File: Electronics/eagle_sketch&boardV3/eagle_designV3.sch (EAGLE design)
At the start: 16 parts, among them IC1 7805L

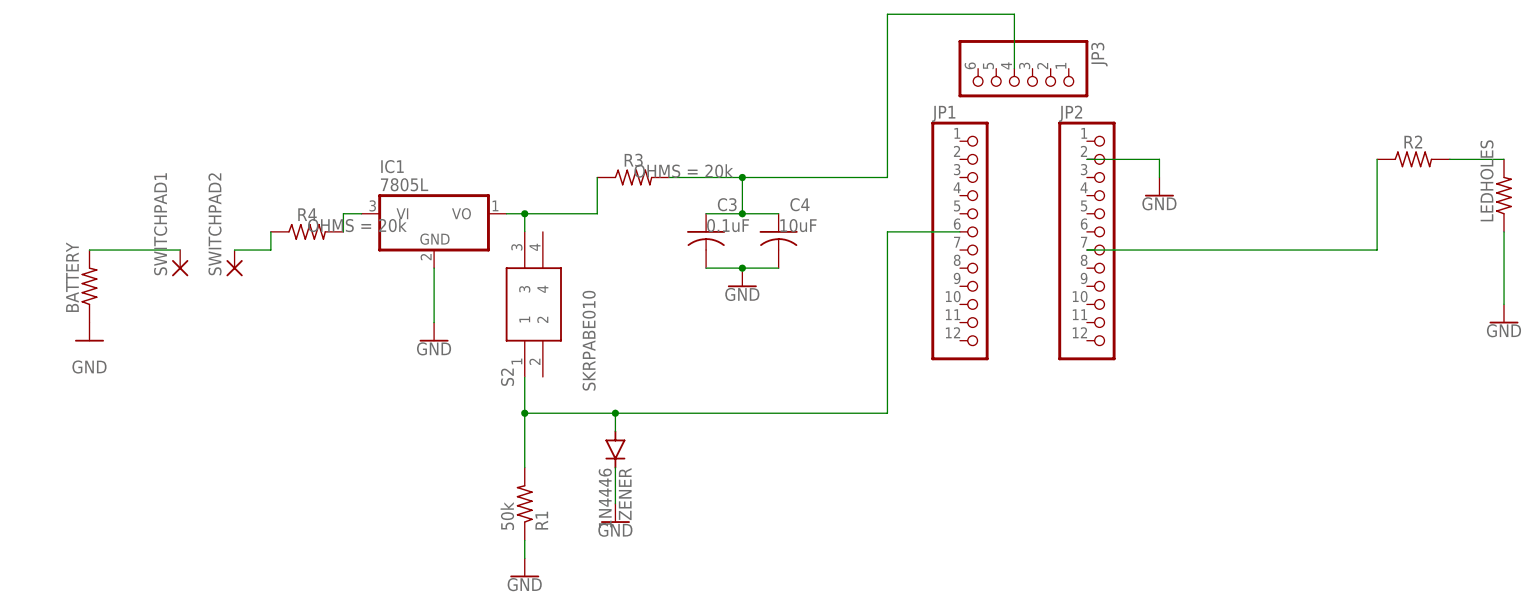
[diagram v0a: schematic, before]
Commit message: updated board and schematic with post review suggestions from Issue 30
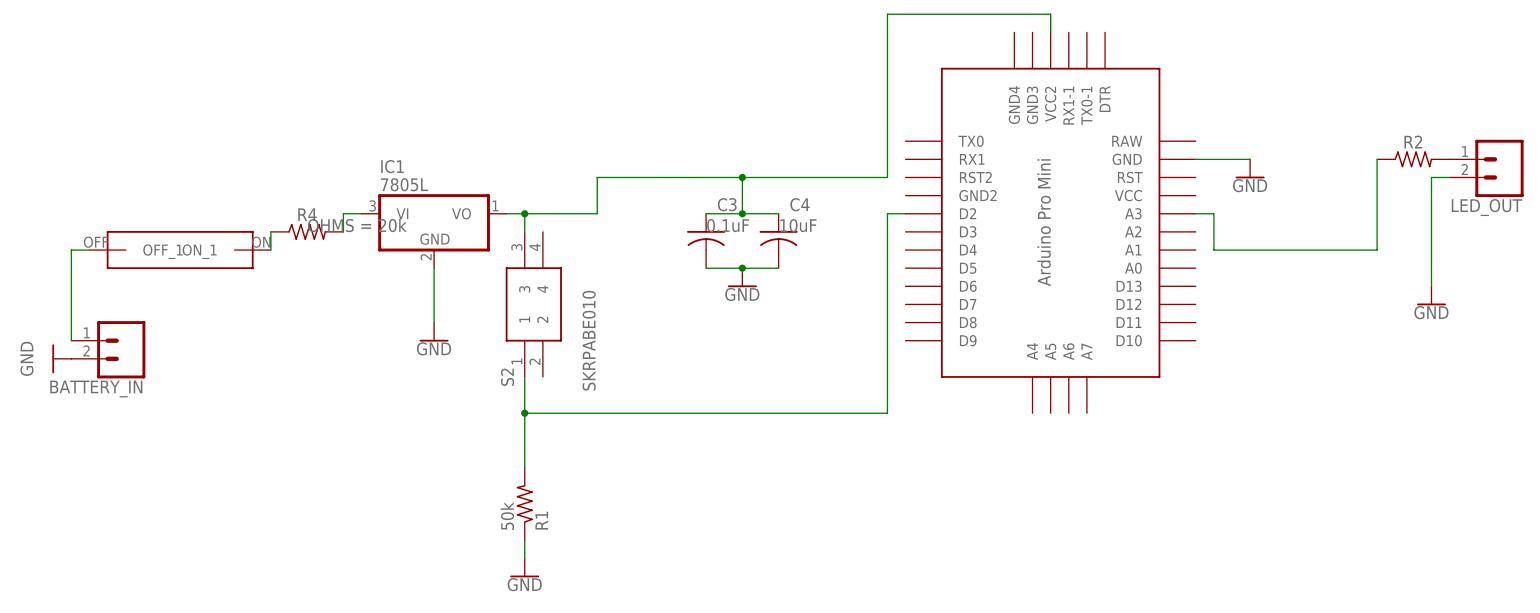
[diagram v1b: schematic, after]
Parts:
- removed BATTERY: (no value), adafruit:R-US_0411/12
- removed JP1, JP2: (no value), adafruit:PINHD-1X12
- removed JP3: (no value), adafruit:PINHD-1X6
- removed LEDHOLES: (no value), adafruit:R-US_0309/12
- removed R3: 20k, adafruit:R-US_R0805
- removed SWITCHPAD1, SWITCHPAD2: (no value), wirepad:SMD2
- removed ZENER: 1N4446, diode:1N4446
- added BATTERY_IN, LED_OUT: (no value), SparkFun-Connectors:CONN_02
- added U$1: PRO-MINI, Arduino-clone:PRO-MINI
- added U$2: SDA01H1SBD_DEVICE, DIPswitchLib:SDA01H1SBD_DEVICE
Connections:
- removed net N$6: C3.1, C4.1, JP3.4, R3.2
- removed net N$9: LEDHOLES.2, R2.2
- new net N$7: LED_OUT.1, R2.2
- net GND: now also BATTERY_IN.2, LED_OUT.2, U$1.GND; no longer BATTERY.1, JP2.2, LEDHOLES.1, ZENER.C
- net N$1: now also BATTERY_IN.1, U$2.OFF_1; no longer BATTERY.2, SWITCHPAD1.P
- net N$2: now also U$2.ON_1; no longer SWITCHPAD2.P
- net N$4: now also C3.1, C4.1, U$1.VCC2; no longer R3.1
- net N$5: now also U$1.D2; no longer JP1.6, ZENER.A
- net N$8: now also U$1.A3; no longer JP2.7

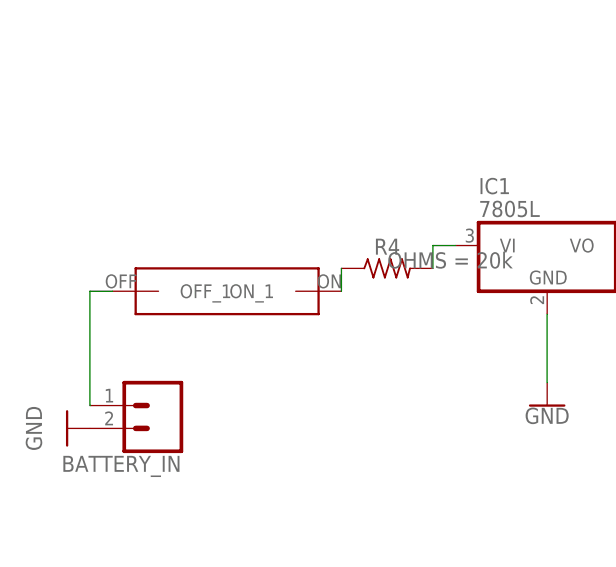
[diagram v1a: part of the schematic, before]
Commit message: updated board to reflect toggle switch change
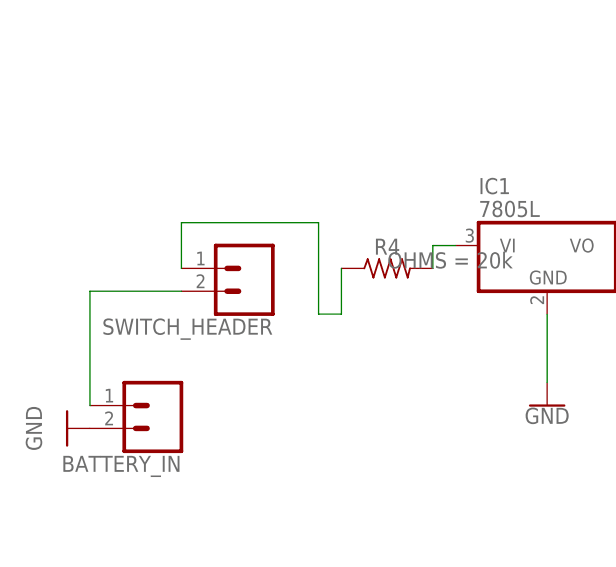
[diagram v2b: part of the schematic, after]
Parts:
- removed U$2: SDA01H1SBD_DEVICE, DIPswitchLib:SDA01H1SBD_DEVICE
- added SWITCH_HEADER: (no value), SparkFun-Connectors:CONN_02
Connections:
- net N$1: now also SWITCH_HEADER.2; no longer U$2.OFF_1
- net N$2: now also SWITCH_HEADER.1; no longer U$2.ON_1
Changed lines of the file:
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@@
 <part name="GND6" library="SparkFun-PowerSymbols" library_urn="urn:adsk.eagle:library:530" deviceset="GND" device=""/>
 <part name="U$1" library="Arduino-clone" deviceset="PRO-MINI" device=""/>
-<part name="U$2" library="DIPswitchLib" deviceset="SDA01H1SBD_DEVICE" device=""/>
 <part name="BATTERY_IN" library="SparkFun-Connectors" library_urn="urn:adsk.eagle:library:513" deviceset="CONN_02" device="" package3d_urn="urn:adsk.eagle:package:38039/1"/>
 <part name="LED_OUT" library="SparkFun-Connectors" library_urn="urn:adsk.eagle:library:513" deviceset="CONN_02" device="" package3d_urn="urn:adsk.eagle:package:38039/1"/>
+<part name="SWITCH_HEADER" library="SparkFun-Connectors" library_urn="urn:adsk.eagle:library:513" deviceset="CONN_02" device="" package3d_urn="urn:adsk.eagle:package:38039/1"/>
 </parts>
 <sheets>
@@
 </instance>
 <instance part="U$1" gate="G$1" x="144.78" y="53.34" smashed="yes"/>
-<instance part="U$2" gate="G$1" x="20.32" y="58.42" smashed="yes"/>
 <instance part="BATTERY_IN" gate="G$1" x="12.7" y="45.72" smashed="yes" rot="R180">
 <attribute name="VALUE" x="15.24" y="50.546" size="1.778" layer="96" font="vector" rot="R180"/>
@@
 <attribute name="NAME" x="208.28" y="65.532" size="1.778" layer="95" font="vector" rot="R180"/>
 </instance>
+<instance part="SWITCH_HEADER" gate="G$1" x="22.86" y="60.96" smashed="yes" rot="R180">
+<attribute name="VALUE" x="25.4" y="65.786" size="1.778" layer="96" font="vector" rot="R180"/>
+<attribute name="NAME" x="25.4" y="55.372" size="1.778" layer="95" font="vector" rot="R180"/>
+</instance>
 </instances>
 <busses>
@@
 <segment>
 <pinref part="R4" gate="G$1" pin="1"/>
-<wire x1="33.02" y1="58.42" x2="33.02" y2="60.96" width="0.1524" layer="91"/>
-<pinref part="U$2" gate="G$1" pin="ON_1"/>
+<pinref part="SWITCH_HEADER" gate="G$1" pin="1"/>
+<wire x1="15.24" y1="60.96" x2="15.24" y2="66.04" width="0.1524" layer="91"/>
+<wire x1="15.24" y1="66.04" x2="30.48" y2="66.04" width="0.1524" layer="91"/>
+<wire x1="30.48" y1="66.04" x2="30.48" y2="55.88" width="0.1524" layer="91"/>
+<wire x1="30.48" y1="55.88" x2="33.02" y2="55.88" width="0.1524" layer="91"/>
+<wire x1="33.02" y1="55.88" x2="33.02" y2="60.96" width="0.1524" layer="91"/>
 </segment>
 </net>
@@
 <pinref part="BATTERY_IN" gate="G$1" pin="1"/>
 <wire x1="5.08" y1="45.72" x2="5.08" y2="58.42" width="0.1524" layer="91"/>
-<pinref part="U$2" gate="G$1" pin="OFF_1"/>
-<wire x1="5.08" y1="58.42" x2="7.62" y2="58.42" width="0.1524" layer="91"/>
+<pinref part="SWITCH_HEADER" gate="G$1" pin="2"/>
+<wire x1="5.08" y1="58.42" x2="15.24" y2="58.42" width="0.1524" layer="91"/>
 </segment>
 </net>

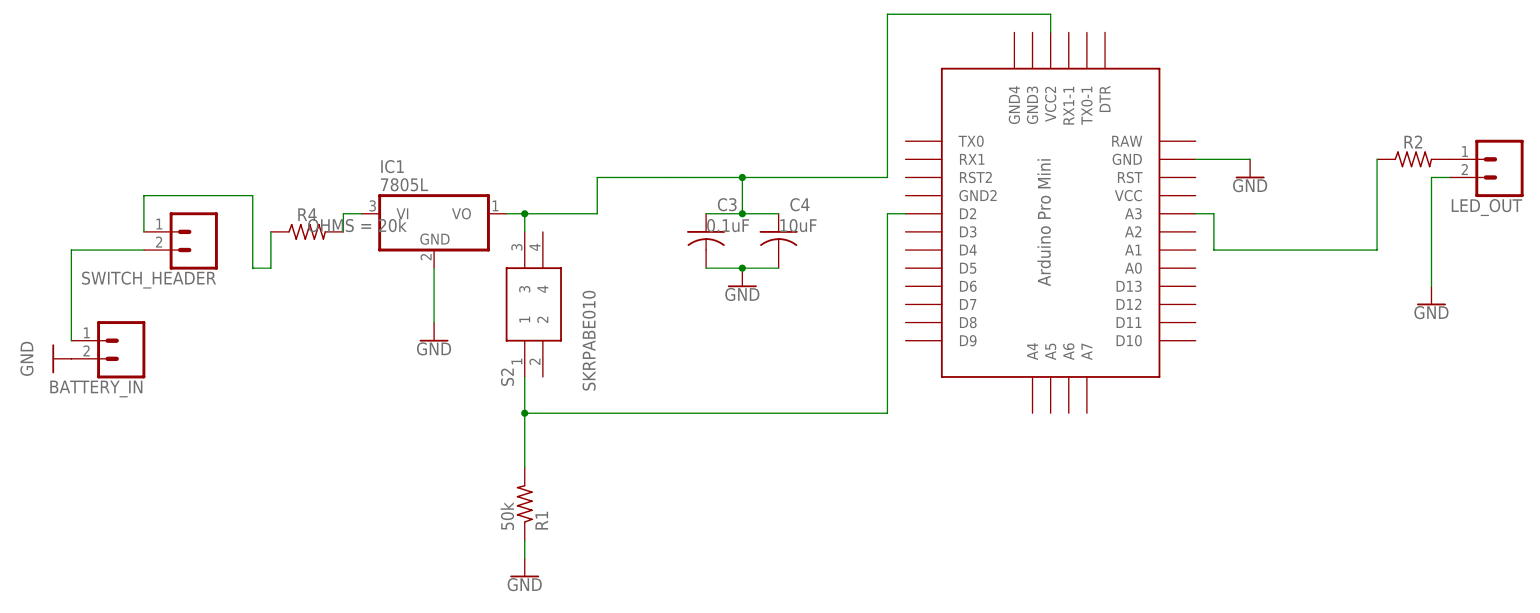
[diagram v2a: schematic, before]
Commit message: updated board and schematic to reflect removal of resistor btwn battery and voltage reg
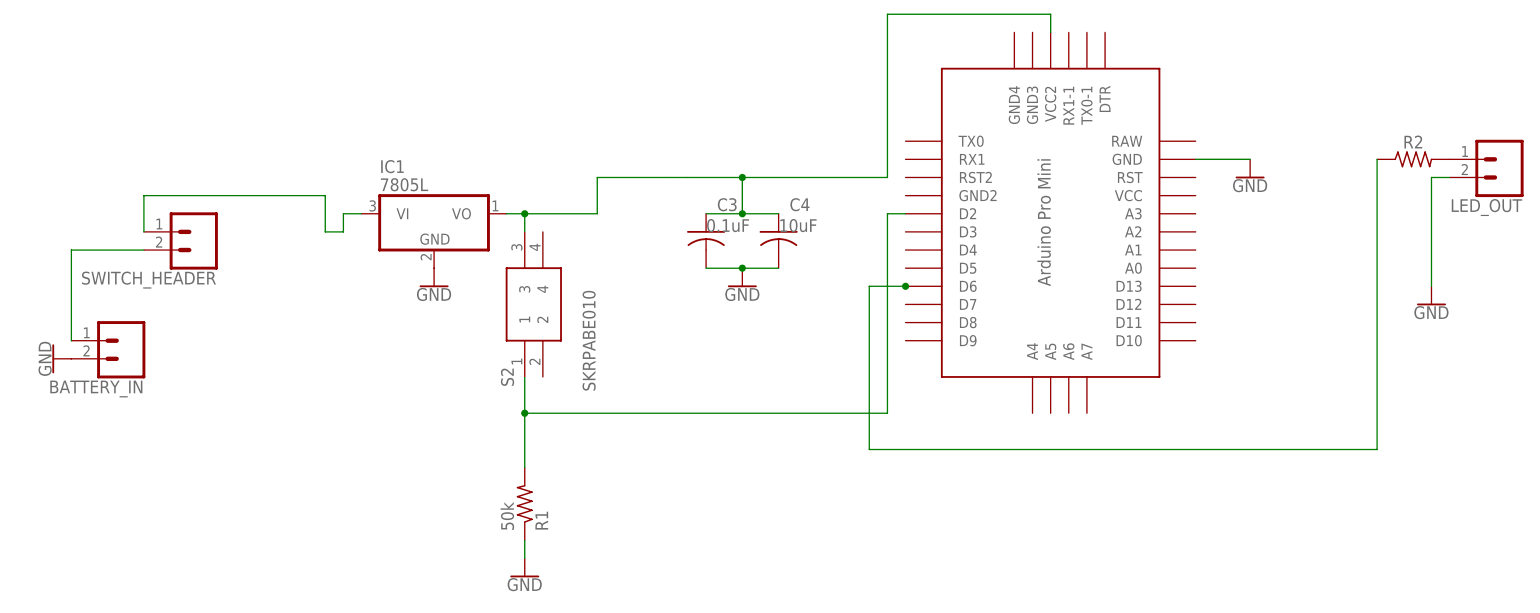
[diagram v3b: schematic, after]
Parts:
- removed R4: 20k, adafruit:R-US_R0805
- R2: value 1.5k -> 330
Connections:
- removed net N$3: IC1.VI, R4.2
- removed net N$8: R2.1, U$1.A3
- new net N$6: R2.1, U$1.D6
- net N$2: now also IC1.VI; no longer R4.1
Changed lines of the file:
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@@
 <part name="R1" library="adafruit" library_urn="urn:adsk.eagle:library:420" deviceset="R-US_" device="R0805" package3d_urn="urn:adsk.eagle:package:6240566/1" value="50k"/>
 <part name="S2" library="SKRPABE010" deviceset="SKRPABE010" device=""/>
-<part name="R2" library="adafruit" library_urn="urn:adsk.eagle:library:420" deviceset="R-US_" device="R0805" package3d_urn="urn:adsk.eagle:package:6240566/1" value="1.5k"/>
-<part name="GND1" library="SparkFun-PowerSymbols" library_urn="urn:adsk.eagle:library:530" deviceset="GND" device=""/>
-<part name="R4" library="adafruit" library_urn="urn:adsk.eagle:library:420" deviceset="R-US_" device="R0805" package3d_urn="urn:adsk.eagle:package:6240566/1" value="20k">
-<attribute name="OHMS" value="20k"/>
-</part>
+<part name="R2" library="adafruit" library_urn="urn:adsk.eagle:library:420" deviceset="R-US_" device="R0805" package3d_urn="urn:adsk.eagle:package:6240566/1" value="330"/>
 <part name="GND4" library="SparkFun-PowerSymbols" library_urn="urn:adsk.eagle:library:530" deviceset="GND" device=""/>
 <part name="C3" library="adafruit" library_urn="urn:adsk.eagle:library:420" deviceset="C-US" device="C0805" package3d_urn="urn:adsk.eagle:package:6240337/1" value="0.1uF">
@@
 <part name="LED_OUT" library="SparkFun-Connectors" library_urn="urn:adsk.eagle:library:513" deviceset="CONN_02" device="" package3d_urn="urn:adsk.eagle:package:38039/1"/>
 <part name="SWITCH_HEADER" library="SparkFun-Connectors" library_urn="urn:adsk.eagle:library:513" deviceset="CONN_02" device="" package3d_urn="urn:adsk.eagle:package:38039/1"/>
+<part name="GND1" library="SparkFun-PowerSymbols" library_urn="urn:adsk.eagle:library:530" deviceset="GND" device=""/>
 </parts>
 <sheets>
@@
 <instance part="R2" gate="G$1" x="193.04" y="71.12" smashed="yes">
 <attribute name="NAME" x="193.04" y="72.644" size="1.778" layer="95" font="vector" align="bottom-center"/>
-</instance>
-<instance part="GND1" gate="1" x="2.54" y="43.18" smashed="yes" rot="R270">
-<attribute name="VALUE" x="-0.254" y="43.18" size="1.778" layer="96" rot="R270" align="top-center"/>
-</instance>
-<instance part="R4" gate="G$1" x="38.1" y="60.96" smashed="yes">
-<attribute name="NAME" x="38.1" y="62.484" size="1.778" layer="95" font="vector" align="bottom-center"/>
-<attribute name="OHMS" x="38.1" y="60.96" size="1.778" layer="96" display="both"/>
 </instance>
 <instance part="GND4" gate="1" x="68.58" y="12.7" smashed="yes">
@@
 <attribute name="VALUE" x="48.26" y="66.675" size="1.778" layer="96"/>
 </instance>
-<instance part="GND3" gate="1" x="55.88" y="45.72" smashed="yes">
-<attribute name="VALUE" x="55.88" y="45.466" size="1.778" layer="96" align="top-center"/>
+<instance part="GND3" gate="1" x="55.88" y="53.34" smashed="yes">
+<attribute name="VALUE" x="55.88" y="53.086" size="1.778" layer="96" align="top-center"/>
 </instance>
 <instance part="GND6" gate="1" x="99.06" y="53.34" smashed="yes">
@@
 <attribute name="NAME" x="25.4" y="55.372" size="1.778" layer="95" font="vector" rot="R180"/>
 </instance>
+<instance part="GND1" gate="1" x="2.54" y="43.18" smashed="yes" rot="R270">
+<attribute name="VALUE" x="2.286" y="43.18" size="1.778" layer="96" rot="R270" align="top-center"/>
+</instance>
 </instances>
 <busses>
@@
 <net name="N$2" class="0">
 <segment>
-<pinref part="R4" gate="G$1" pin="1"/>
 <pinref part="SWITCH_HEADER" gate="G$1" pin="1"/>
 <wire x1="15.24" y1="60.96" x2="15.24" y2="66.04" width="0.1524" layer="91"/>
-<wire x1="15.24" y1="66.04" x2="30.48" y2="66.04" width="0.1524" layer="91"/>
-<wire x1="30.48" y1="66.04" x2="30.48" y2="55.88" width="0.1524" layer="91"/>
-<wire x1="30.48" y1="55.88" x2="33.02" y2="55.88" width="0.1524" layer="91"/>
-<wire x1="33.02" y1="55.88" x2="33.02" y2="60.96" width="0.1524" layer="91"/>
-</segment>
-</net>
-<net name="N$3" class="0">
-<segment>
+<wire x1="15.24" y1="66.04" x2="40.64" y2="66.04" width="0.1524" layer="91"/>
+<wire x1="40.64" y1="66.04" x2="40.64" y2="60.96" width="0.1524" layer="91"/>
 <pinref part="IC1" gate="A1" pin="VI"/>
-<pinref part="R4" gate="G$1" pin="2"/>
 <wire x1="45.72" y1="63.5" x2="43.18" y2="63.5" width="0.1524" layer="91"/>
 <wire x1="43.18" y1="63.5" x2="43.18" y2="60.96" width="0.1524" layer="91"/>
+<wire x1="40.64" y1="60.96" x2="43.18" y2="60.96" width="0.1524" layer="91"/>
 </segment>
 </net>
 <net name="GND" class="0">
-<segment>
-<pinref part="IC1" gate="A1" pin="GND"/>
-<pinref part="GND3" gate="1" pin="GND"/>
-<wire x1="55.88" y1="55.88" x2="55.88" y2="48.26" width="0.1524" layer="91"/>
-</segment>
 <segment>
 <pinref part="R1" gate="G$1" pin="1"/>
@@
 </segment>
 <segment>
-<pinref part="BATTERY_IN" gate="G$1" pin="2"/>
-<pinref part="GND1" gate="1" pin="GND"/>
-</segment>
-<segment>
 <pinref part="LED_OUT" gate="G$1" pin="2"/>
 <wire x1="198.12" y1="68.58" x2="195.58" y2="68.58" width="0.1524" layer="91"/>
 <wire x1="195.58" y1="68.58" x2="195.58" y2="53.34" width="0.1524" layer="91"/>
 <pinref part="GND8" gate="1" pin="GND"/>
+</segment>
+<segment>
+<pinref part="GND1" gate="1" pin="GND"/>
+<pinref part="BATTERY_IN" gate="G$1" pin="2"/>
+</segment>
+<segment>
+<pinref part="IC1" gate="A1" pin="GND"/>
+<pinref part="GND3" gate="1" pin="GND"/>
 </segment>
 </net>
@@
 </segment>
 </net>
-<net name="N$8" class="0">
-<segment>
-<wire x1="187.96" y1="58.42" x2="187.96" y2="71.12" width="0.1524" layer="91"/>
-<pinref part="R2" gate="G$1" pin="1"/>
-<wire x1="187.96" y1="58.42" x2="165.1" y2="58.42" width="0.1524" layer="91"/>
-<wire x1="165.1" y1="58.42" x2="165.1" y2="63.5" width="0.1524" layer="91"/>
-<pinref part="U$1" gate="G$1" pin="A3"/>
-<wire x1="165.1" y1="63.5" x2="162.56" y2="63.5" width="0.1524" layer="91"/>
-</segment>
-</net>
 <net name="N$1" class="0">
 <segment>
@@
 </segment>
 </net>
+<net name="N$6" class="0">
+<segment>
+<pinref part="U$1" gate="G$1" pin="D6"/>
+<junction x="121.92" y="53.34"/>
+<wire x1="121.92" y1="53.34" x2="116.84" y2="53.34" width="0.1524" layer="91"/>
+<wire x1="116.84" y1="53.34" x2="116.84" y2="30.48" width="0.1524" layer="91"/>
+<pinref part="R2" gate="G$1" pin="1"/>
+<wire x1="116.84" y1="30.48" x2="187.96" y2="30.48" width="0.1524" layer="91"/>
+<wire x1="187.96" y1="30.48" x2="187.96" y2="71.12" width="0.1524" layer="91"/>
+</segment>
+</net>
